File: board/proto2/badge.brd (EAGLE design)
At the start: 136.5 x 119 mm, 65 parts, among them IC1 TLV62569, J1 5051101092, J2 M05X2X1.27

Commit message: Preliminary routing done
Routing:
- net +3V3: track 112.1 -> 126.4 mm, vias 20 -> 21
- net GND: track 121.1 -> 124.4 mm
- net VBAT: track 181.6 -> 180.6 mm
- net P0.03: track 46.7 -> 47.6 mm
- net P0.12: track 57.3 -> 58.0 mm

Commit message: goffing around with artwork
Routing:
- net VBAT: track 180.6 -> 150.9 mm
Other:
- board text added: "#badgelife JoCo Badge Team:"
- board text added: "AI4QR"
- board text added: "AI6TK"
- board text added: "AI6ZU"
- board text added: "EXPANSION"
- board text added: "N5AC"
- board text added: "W5NYV"

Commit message: remove unneeded pin labels
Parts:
- JP1: value (none) -> NP
- U1: value (none) -> BMD-300
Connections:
- removed net P0.15: U1.P33
- removed net P0.16: U1.P34
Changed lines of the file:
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@@
 </autorouter>
 <elements>
-<element name="U1" library="BMD-300" package="BMD-300" value="" x="105.89691875" y="71.377684375" smashed="yes" rot="R332">
+<element name="U1" library="BMD-300" package="BMD-300" value="BMD-300" x="105.89691875" y="71.377684375" smashed="yes" rot="R332">
 <attribute name="NAME" x="113.5096625" y="75.25790625" size="1.27" layer="51" rot="R332" align="center"/>
 <attribute name="NAME" x="111.06475625" y="82.4947" size="0.8128" layer="25" font="vector" rot="R62" align="bottom-right"/>
@@
 <attribute name="VALUE" x="88.488" y="91.978" size="1.27" layer="27"/>
 </element>
-<element name="JP1" library="pinhead" package="2X04" value="" x="22.606" y="71.628" smashed="yes" rot="R270">
+<element name="JP1" library="pinhead" package="2X04" value="NP" x="22.606" y="71.628" smashed="yes" rot="R270">
 <attribute name="NAME" x="25.781" y="76.708" size="0.8128" layer="25" font="vector" ratio="10" rot="R270"/>
 <attribute name="VALUE" x="18.161" y="76.708" size="1.27" layer="27" rot="R270"/>
@@
 <wire x1="113.284" y1="63.246" x2="110.744" y2="63.246" width="0.254" layer="16"/>
 </signal>
-<signal name="P0.15">
-<contactref element="U1" pad="P33"/>
-</signal>
-<signal name="P0.16">
-<contactref element="U1" pad="P34"/>
-</signal>
 <signal name="P0.11">

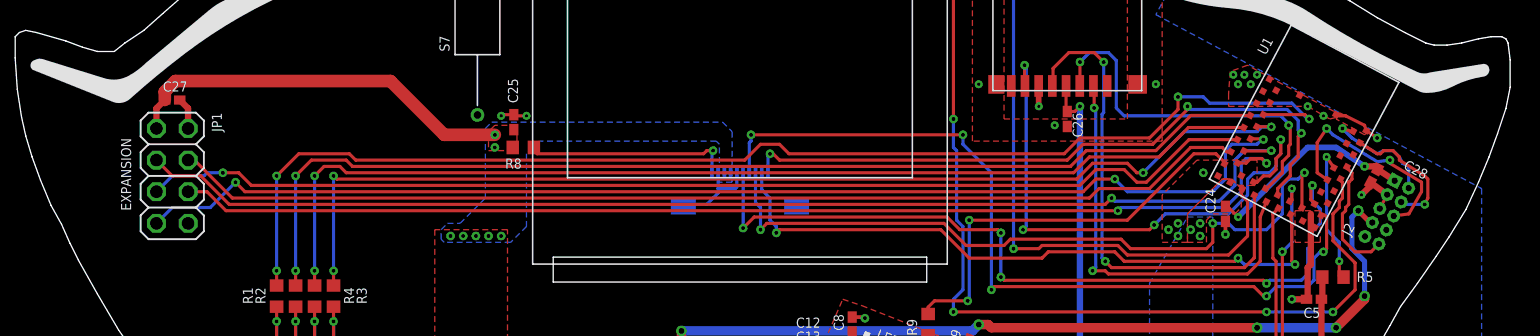
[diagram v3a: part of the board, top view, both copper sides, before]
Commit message: added lanyard holes; thanks to AND\!XOR
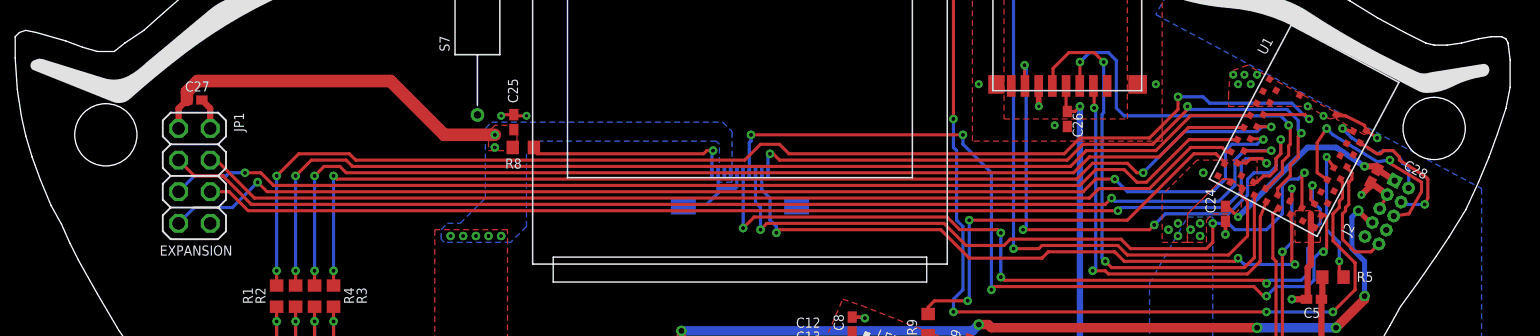
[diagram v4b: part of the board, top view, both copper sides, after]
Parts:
- moved C27 1.78 mm to (24.4, 77.7)
- moved JP1 1.78 mm to (24.4, 71.6)
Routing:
- net P0.30: track 90.2 -> 88.4 mm
- net P0.31: track 96.4 -> 94.6 mm
- net P0.29: track 95.5 -> 93.8 mm
- net P0.01: track 93.1 -> 91.3 mm
- net P0.00: track 86.8 -> 85.1 mm
- net +3V3: track 126.4 -> 124.7 mm
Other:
- board text added: "Special thanks to team AND\!XOR"
